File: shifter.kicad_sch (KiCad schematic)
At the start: 11 parts

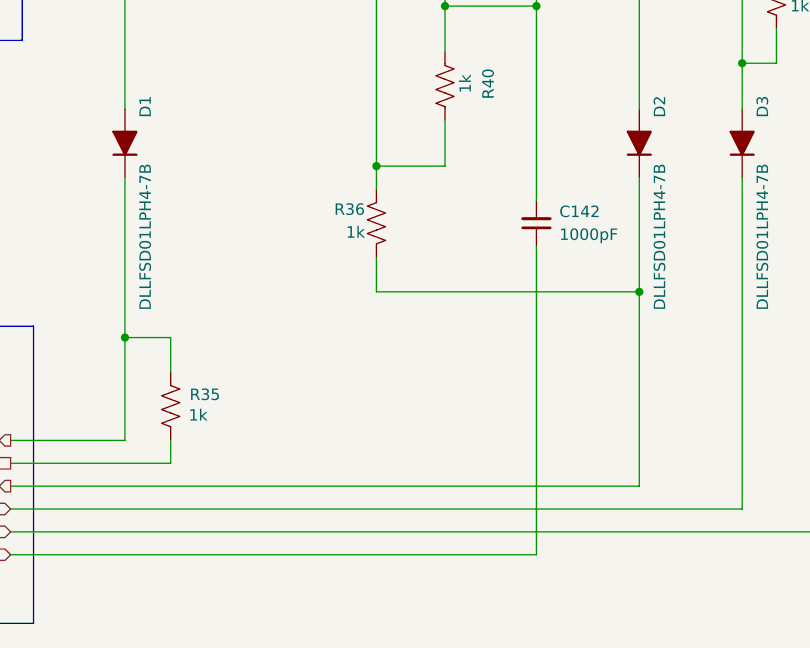
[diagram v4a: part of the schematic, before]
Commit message: TX_IN modified to pull low to GND_L in level shifter (Closes: #2)
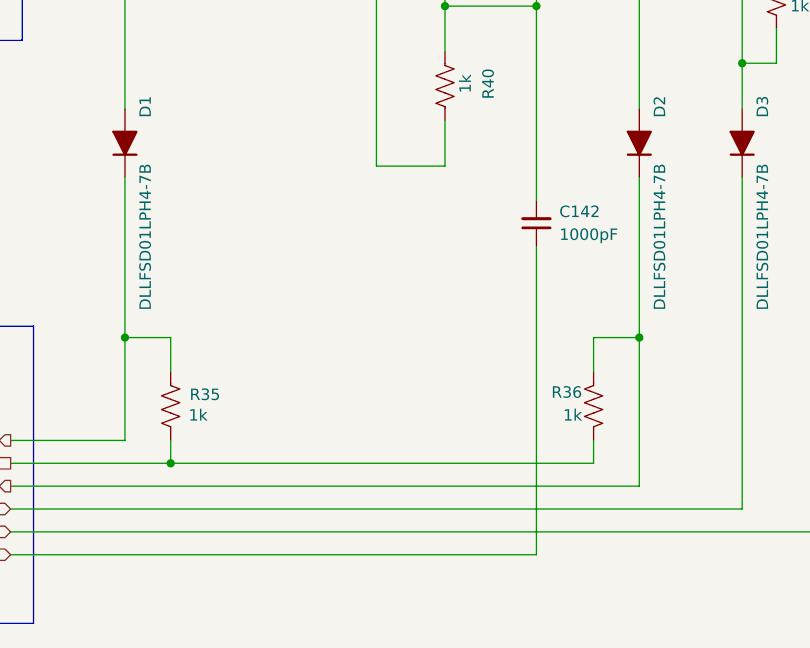
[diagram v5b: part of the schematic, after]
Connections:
- net GND_H: no longer R36.1
- net GND_L: now also R36.2
- net TX_IN: now also R36.1; no longer R36.2
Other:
- moved on the sheet: R36
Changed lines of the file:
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@@
 	)
 	(junction
-		(at 121.92 86.36)
-		(diameter 0)
-		(color 0 0 0 0)
-	)
-	(junction
-		(at 151.13 100.33)
+		(at 99.06 119.38)
 		(diameter 0)
 		(color 0 0 0 0)
@@
 	)
 	(junction
+		(at 151.13 105.41)
+		(diameter 0)
+		(color 0 0 0 0)
+	)
+	(junction
 		(at 162.56 74.93)
 		(diameter 0)
@@
 		)
 	)
+	(wire
+		(pts
+			(xy 146.05 109.22) (xy 146.05 105.41)
+		)
+		(stroke
+			(width 0)
+			(type default)
+		)
+	)
 	(polyline
 		(pts
@@
 	(wire
 		(pts
+			(xy 146.05 105.41) (xy 151.13 105.41)
+		)
+		(stroke
+			(width 0)
+			(type default)
+		)
+	)
+	(wire
+		(pts
 			(xy 166.37 74.93) (xy 162.56 74.93)
 		)
@@
 	(wire
 		(pts
-			(xy 121.92 100.33) (xy 151.13 100.33)
-		)
-		(stroke
-			(width 0)
-			(type default)
-		)
-	)
-	(wire
-		(pts
-			(xy 151.13 87.63) (xy 151.13 100.33)
-		)
-		(stroke
-			(width 0)
-			(type default)
-		)
-	)
-	(wire
-		(pts
 			(xy 99.06 116.84) (xy 99.06 119.38)
 		)
@@
 	(wire
 		(pts
+			(xy 151.13 105.41) (xy 151.13 121.92)
+		)
+		(stroke
+			(width 0)
+			(type default)
+		)
+	)
+	(wire
+		(pts
 			(xy 121.92 55.88) (xy 121.92 86.36)
 		)
@@
 	(wire
 		(pts
-			(xy 121.92 86.36) (xy 121.92 88.9)
-		)
-		(stroke
-			(width 0)
-			(type default)
-		)
-	)
-	(wire
-		(pts
 			(xy 80.01 53.34) (xy 151.13 53.34)
 		)
@@
 	(wire
 		(pts
+			(xy 99.06 119.38) (xy 146.05 119.38)
+		)
+		(stroke
+			(width 0)
+			(type default)
+		)
+	)
+	(wire
+		(pts
 			(xy 80.01 43.18) (xy 129.54 43.18)
 		)
@@
 	(wire
 		(pts
+			(xy 146.05 119.38) (xy 146.05 116.84)
+		)
+		(stroke
+			(width 0)
+			(type default)
+		)
+	)
+	(wire
+		(pts
 			(xy 139.7 45.72) (xy 139.7 68.58)
 		)
@@
 	(wire
 		(pts
-			(xy 121.92 96.52) (xy 121.92 100.33)
-		)
-		(stroke
-			(width 0)
-			(type default)
-		)
-	)
-	(wire
-		(pts
 			(xy 175.26 80.01) (xy 175.26 74.93)
 		)
@@
 	(wire
 		(pts
-			(xy 151.13 100.33) (xy 151.13 121.92)
+			(xy 151.13 87.63) (xy 151.13 105.41)
 		)
 		(stroke
@@
 	(symbol
 		(lib_id "Device:R_US")
-		(at 121.92 92.71 0)
+		(at 146.05 113.03 0)
 		(mirror y)
 		(unit 1)
@@
 		(dnp no)
 		(property "Reference" "R36"
-			(at 120.65 91.186 0)
+			(at 144.78 111.506 0)
 			(effects
 				(font
@@
 		)
 		(property "Value" "1k"
-			(at 120.65 93.726 0)
+			(at 144.78 114.046 0)
 			(effects
 				(font
@@
 		)
 		(property "Footprint" "Resistor_SMD:R_0402_1005Metric"
-			(at 120.904 92.964 90)
+			(at 145.034 113.284 90)
 			(effects
 				(font
@@
 		)
 		(property "Datasheet" "~"
-			(at 121.92 92.71 0)
+			(at 146.05 113.03 0)
 			(effects
 				(font
@@
 		)
 		(property "Description" "Resistor, US symbol"
-			(at 121.92 92.71 0)
+			(at 146.05 113.03 0)
 			(effects
 				(font
@@
 		)
 		(property "DK" "311-1.00KLRCT-ND"
-			(at 121.92 92.71 0)
+			(at 146.05 113.03 0)
 			(effects
 				(font
@@
 		)
 		(property "PARTNO" "RC0402FR-071KL"
-			(at 121.92 92.71 0)
+			(at 146.05 113.03 0)
 			(effects
 				(font
@@
 		)
 		(property "Mouser" ""
-			(at 121.92 92.71 0)
+			(at 146.05 113.03 0)
 			(effects
 				(font
@@
 		)
 		(property "Manufacturer" ""
-			(at 121.92 92.71 0)
-			(effects
-				(font
+			(at 146.05 113.03 0)
+			(effects
+				(font
